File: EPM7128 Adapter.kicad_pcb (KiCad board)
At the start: 2 copper layers, 76 x 82.6 mm, 17 parts

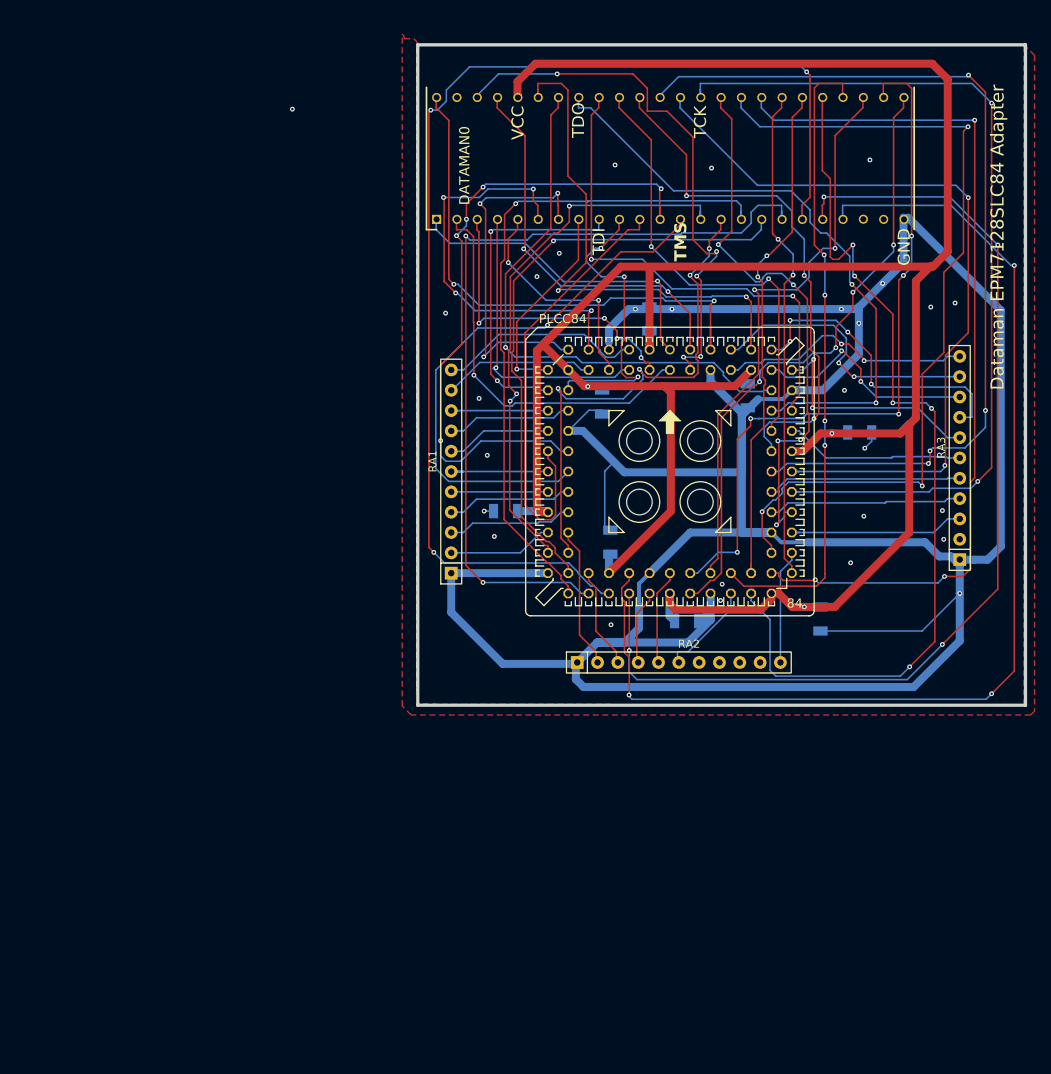
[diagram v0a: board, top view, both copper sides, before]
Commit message: Add files via upload
Correct issue with lack of Gnd connection to JTAG, RNETs and PLCC Socket.
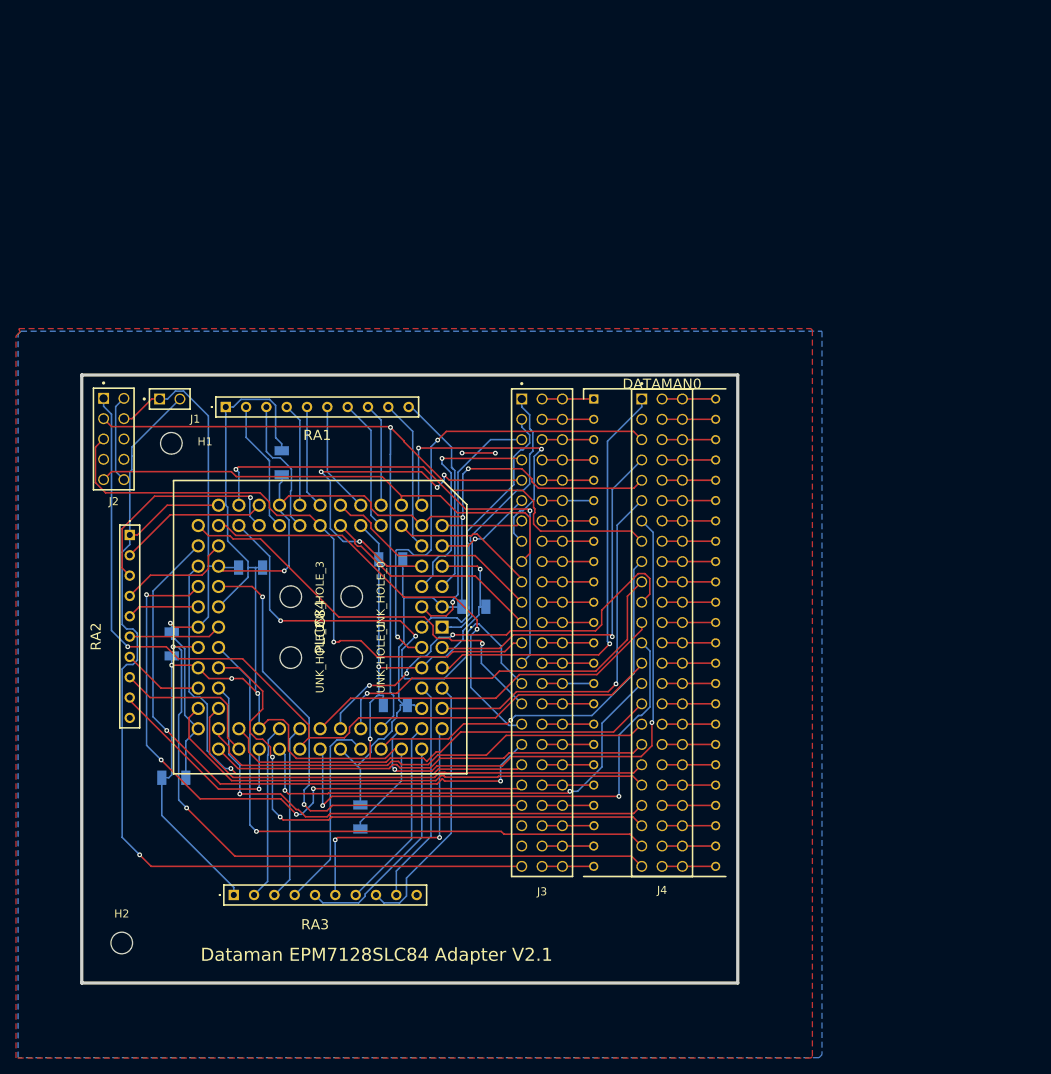
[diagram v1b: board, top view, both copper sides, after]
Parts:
- added H1: MountingHole, MountingHole:MountingHole_2.7mm_M2.5, F.Cu at (79.2, 113.5)
- added H2: MountingHole, MountingHole:MountingHole_2.7mm_M2.5, F.Cu at (73.0, 176.0)
- added J1: Conn_01x02, Mod:SAMTEC_TSW-102-07-G-S, F.Cu at (79.0, 108.0)
- added J2: Conn_02x05_Odd_Even, Mod:SAMTEC_TSW-105-07-L-D, F.Cu at (72.0, 113.0)
- added J3: TSW-124-08-T-T, Mod:SAMTEC_TSW-124-08-T-T, F.Cu at (123.0, 108.0)
- added J4: TSW-124-08-T-T, Mod:SAMTEC_TSW-124-08-T-T, F.Cu at (138.0, 108.0)
- DATAMAN0: value ~ -> Pin-Pin Headers 1x24
- PLCC84: footprint S84 -> Mod:PLCC84AT
- RA1, RA2, RA3: footprint Resistor_THT:R_Array_SIP11 -> Mod:4610M101103LF
- UNK_HOLE_0: value ~ -> Extraction Hole; footprint dummyfp0 -> MountingHole:MountingHole_2.7mm_M2.5
- UNK_HOLE_1: value ~ -> Extraction Hole; footprint dummyfp1 -> MountingHole:MountingHole_2.7mm_M2.5
- UNK_HOLE_2: value ~ -> Extraction Hole; footprint dummyfp2 -> MountingHole:MountingHole_2.7mm_M2.5
- UNK_HOLE_3: value ~ -> Extraction Hole; footprint dummyfp3 -> MountingHole:MountingHole_2.7mm_M2.5
- moved RA3 100.0 mm to (87.0, 170.0), turned to 0 degrees
- moved C4 83.2 mm to (79.5, 155.3), turned to 180 degrees
- moved C5 78.8 mm to (102.8, 160.2), turned to -90 degrees
- moved C6 64.4 mm to (79.2, 138.6), turned to -90 degrees
- moved C1 58.6 mm to (107.2, 146.3), turned to 180 degrees
- moved RA2 58.2 mm to (74.0, 125.0), turned to -90 degrees
- moved UNK_HOLE_2 54.8 mm to (94.1, 140.3), turned to -90 degrees
- moved UNK_HOLE_1 51.3 mm to (101.7, 140.3), turned to -90 degrees
- moved UNK_HOLE_3 45.2 mm to (94.1, 132.7), turned to -90 degrees
- moved C3 45.1 mm to (89.1, 129.1), turned to 0 degrees
- moved C8 42.1 mm to (117.0, 134.0), turned to 0 degrees
- moved UNK_HOLE_0 40.9 mm to (101.7, 132.7), turned to -90 degrees
- moved RA1 35.0 mm to (86.0, 109.0), turned to 0 degrees
- moved PLCC84 34.5 mm to (113.0, 136.5), turned to -90 degrees
- moved C2 32.9 mm to (106.6, 128.0), turned to 180 degrees
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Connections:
- DATAMAN0 pad 1: GLCRn -> Net-(DATAMAN0-Pad1)
- DATAMAN0 pad 10: IO15 -> Net-(DATAMAN0-Pad10)
- DATAMAN0 pad 11: IO20 -> Net-(DATAMAN0-Pad11)
- DATAMAN0 pad 12: IO21 -> Net-(DATAMAN0-Pad12)
- DATAMAN0 pad 13: IO23 -> Net-(DATAMAN0-Pad13)
- DATAMAN0 pad 14: IO30 -> Net-(DATAMAN0-Pad14)
- DATAMAN0 pad 15: IO31 -> Net-(DATAMAN0-Pad15)
- DATAMAN0 pad 16: IO33 -> Net-(DATAMAN0-Pad16)
- DATAMAN0 pad 17: IO34 -> Net-(DATAMAN0-Pad17)
- DATAMAN0 pad 18: IO35 -> Net-(DATAMAN0-Pad18)
- DATAMAN0 pad 19: IO37 -> Net-(DATAMAN0-Pad19)
- DATAMAN0 pad 2: OE2n -> Net-(DATAMAN0-Pad2)
- DATAMAN0 pad 20: IO39 -> Net-(DATAMAN0-Pad20)
- DATAMAN0 pad 21: IO40 -> Net-(DATAMAN0-Pad21)
- DATAMAN0 pad 22: unconnected-(DATAMAN0-Pad22) -> Net-(DATAMAN0-Pad22)
- DATAMAN0 pad 23: unconnected-(DATAMAN0-Pad23) -> Net-(DATAMAN0-Pad23)
- DATAMAN0 pad 24: GND -> Net-(DATAMAN0-Pad24)
- DATAMAN0 pad 25: IO45 -> Net-(DATAMAN0-Pad25)
- DATAMAN0 pad 26: IO46 -> Net-(DATAMAN0-Pad26)
- DATAMAN0 pad 27: IO48 -> Net-(DATAMAN0-Pad27)
- DATAMAN0 pad 28: IO50 -> Net-(DATAMAN0-Pad28)
- DATAMAN0 pad 29: IO51 -> Net-(DATAMAN0-Pad29)
- DATAMAN0 pad 3: IO4 -> Net-(DATAMAN0-Pad3)
- DATAMAN0 pad 30: IO52 -> Net-(DATAMAN0-Pad30)
- DATAMAN0 pad 31: IO54 -> Net-(DATAMAN0-Pad31)
- DATAMAN0 pad 32: IO55 -> Net-(DATAMAN0-Pad32)
- DATAMAN0 pad 33: IO57 -> Net-(DATAMAN0-Pad33)
- DATAMAN0 pad 34: IO60 -> Net-(DATAMAN0-Pad34)
- DATAMAN0 pad 35: IO62 -> Net-(DATAMAN0-Pad35)
- DATAMAN0 pad 36: IO64 -> Net-(DATAMAN0-Pad36)
- DATAMAN0 pad 37: IO65 -> Net-(DATAMAN0-Pad37)
- DATAMAN0 pad 38: IO67 -> Net-(DATAMAN0-Pad38)
- DATAMAN0 pad 39: IO69 -> Net-(DATAMAN0-Pad39)
- DATAMAN0 pad 4: IO6 -> Net-(DATAMAN0-Pad4)
- DATAMAN0 pad 40: IO70 -> Net-(DATAMAN0-Pad40)
- DATAMAN0 pad 41: IO71 -> Net-(DATAMAN0-Pad41)
- DATAMAN0 pad 42: IO73 -> Net-(DATAMAN0-Pad42)
- DATAMAN0 pad 43: IO77 -> Net-(DATAMAN0-Pad43)
- DATAMAN0 pad 44: VCC -> Net-(DATAMAN0-Pad44)
- DATAMAN0 pad 45: GCLK -> Net-(DATAMAN0-Pad45)
- DATAMAN0 pad 46: OE1n -> Net-(DATAMAN0-Pad46)
- DATAMAN0 pad 47: unconnected-(DATAMAN0-Pad47) -> Net-(DATAMAN0-Pad47)
- DATAMAN0 pad 48: IO81 -> Net-(DATAMAN0-Pad48)
- DATAMAN0 pad 5: IO8 -> Net-(DATAMAN0-Pad5)
- DATAMAN0 pad 6: IO9 -> Net-(DATAMAN0-Pad6)
- DATAMAN0 pad 7: IO11 -> Net-(DATAMAN0-Pad7)
- DATAMAN0 pad 8: IO12 -> Net-(DATAMAN0-Pad8)
- DATAMAN0 pad 9: IO14 -> Net-(DATAMAN0-Pad9)
- PLCC84 pad 10: Net-(PLCC84-I/O_10) -> RNET-IO10
- PLCC84 pad 16: Net-(PLCC84-I/O_16) -> RNET-IO16
- PLCC84 pad 17: Net-(PLCC84-I/O_17) -> RNET-IO17
- PLCC84 pad 18: Net-(PLCC84-I/O_18) -> RNET-IO18
- PLCC84 pad 22: Net-(PLCC84-I/O_22) -> RNET-IO22
- PLCC84 pad 24: Net-(PLCC84-I/O_24) -> RNET-IO24
- PLCC84 pad 25: Net-(PLCC84-I/O_25) -> RNET-IO25
- PLCC84 pad 27: Net-(PLCC84-I/O_27) -> RNET-IO27
- PLCC84 pad 28: Net-(PLCC84-I/O_28) -> RNET-IO28
- PLCC84 pad 29: IO29 -> RNET-IO29
- PLCC84 pad 36: IO36 -> RNET-IO36
- PLCC84 pad 41: Net-(PLCC84-I/O_41) -> RNET-IO41
- PLCC84 pad 44: Net-(PLCC84-I/O_44) -> RNET-IO44
- PLCC84 pad 49: Net-(PLCC84-I/O_49) -> RNET-IO49
- PLCC84 pad 5: Net-(PLCC84-I/O_5) -> RNET-IO5
- PLCC84 pad 56: Net-(PLCC84-I/O_56) -> RNET-IO56
- PLCC84 pad 58: Net-(PLCC84-I/O_58) -> RNET-IO58
- PLCC84 pad 61: Net-(PLCC84-I/O_61) -> RNET-IO61
- PLCC84 pad 63: Net-(PLCC84-I/O_63) -> RNET-IO63
- PLCC84 pad 68: Net-(PLCC84-I/O_68) -> RNET-IO68
- PLCC84 pad 74: Net-(PLCC84-I/O_74) -> RNET-IO74
- PLCC84 pad 75: Net-(PLCC84-I/O_75) -> RNET-IO75
- PLCC84 pad 76: Net-(PLCC84-I/O_76) -> RNET-IO76
- PLCC84 pad 79: Net-(PLCC84-I/O_79) -> RNET-IO79
- PLCC84 pad 80: Net-(PLCC84-I/O_80) -> RNET-IO80
- RA1 pad 10: Net-(PLCC84-I/O_10) -> RNET-IO5
- RA1 pad 2: Net-(PLCC84-I/O_28) -> RNET-IO27
- RA1 pad 3: Net-(PLCC84-I/O_27) -> RNET-IO25
- RA1 pad 4: Net-(PLCC84-I/O_25) -> RNET-IO24
- RA1 pad 5: Net-(PLCC84-I/O_24) -> RNET-IO22
- RA1 pad 6: Net-(PLCC84-I/O_22) -> RNET-IO18
- RA1 pad 7: Net-(PLCC84-I/O_18) -> RNET-IO17
- RA1 pad 8: Net-(PLCC84-I/O_17) -> RNET-IO16
- RA1 pad 9: Net-(PLCC84-I/O_16) -> RNET-IO10
- RA2 pad 2: IO29 -> RNET-IO28
- RA2 pad 3: IO36 -> RNET-IO29
- RA2 pad 4: Net-(PLCC84-I/O_41) -> RNET-IO36
- RA2 pad 5: Net-(PLCC84-I/O_44) -> RNET-IO41
- RA2 pad 6: Net-(PLCC84-I/O_49) -> RNET-IO44
- RA2 pad 7: unconnected-(RA2-R6-Pad7) -> RNET-IO49
- RA2 pad 8: unconnected-(RA2-R7-Pad8) -> RNET-IO56
- RA2 pad 9: unconnected-(RA2-R8-Pad9) -> RNET-IO58
- RA3 pad 10: Net-(PLCC84-I/O_79) -> unconnected-(RA3-R9-Pad10)
- RA3 pad 2: unconnected-(RA3-R1-Pad2) -> RNET-IO61
- RA3 pad 3: Net-(PLCC84-I/O_58) -> RNET-IO63
- RA3 pad 4: Net-(PLCC84-I/O_61) -> RNET-IO68
- RA3 pad 5: Net-(PLCC84-I/O_63) -> RNET-IO74
- RA3 pad 6: Net-(PLCC84-I/O_68) -> RNET-IO75
- RA3 pad 7: Net-(PLCC84-I/O_74) -> RNET-IO76
- RA3 pad 8: Net-(PLCC84-I/O_75) -> RNET-IO79
- RA3 pad 9: Net-(PLCC84-I/O_76) -> RNET-IO80
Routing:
- net VCC: track 338.2 -> 205.2 mm, vias 3 -> 4
- net IO37: track 148.8 -> 65.9 mm, vias 3 -> 1
- net IO40: track 142.8 -> 62.5 mm, vias 3 -> 2
- net IO65: track 114.4 -> 46.2 mm, vias 4 -> 0
- net GND: track 404.8 -> 344.6 mm, vias 27 -> 9
- net IO21: track 82.3 -> 27.9 mm, vias 5 -> 0
- net IO55: track 112.0 -> 58.2 mm, vias 3 -> 0
- net IO39: track 130.9 -> 78.8 mm
- net IO57: track 106.6 -> 56.4 mm, vias 3 -> 0
- net IO51: track 113.8 -> 63.8 mm, vias 5 -> 0
- net IO9: track 50.9 -> 12.3 mm, vias 4 -> 1
- net Net-(PLCC84-I/O_75): track 38.5 -> 0.00 mm, vias 4 -> 0
- net IO71: track 78.0 -> 114.2 mm, vias 2 -> 1
- net Net-(PLCC84-I/O_79): track 36.1 -> 0.00 mm, vias 2 -> 0
- net IO11: track 44.5 -> 10.2 mm, vias 3 -> 0
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- added copper zone on F.Cu, net VCC
- removed copper zone on F.Cu, net GND
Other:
- board size 76 x 82.6 mm -> 82 x 76 mm
- board text added: "Dataman EPM7128SLC84 Adapter V2.1"
- board text removed: "Dataman EPM7128SLC84 Adapter"
- board text removed: "GND"
- board text removed: "TCK"
- board text removed: "TDI"
- board text removed: "TDO"
- board text removed: "TMS"
- board text removed: "VCC"
